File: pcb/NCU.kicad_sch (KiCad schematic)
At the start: 4 parts

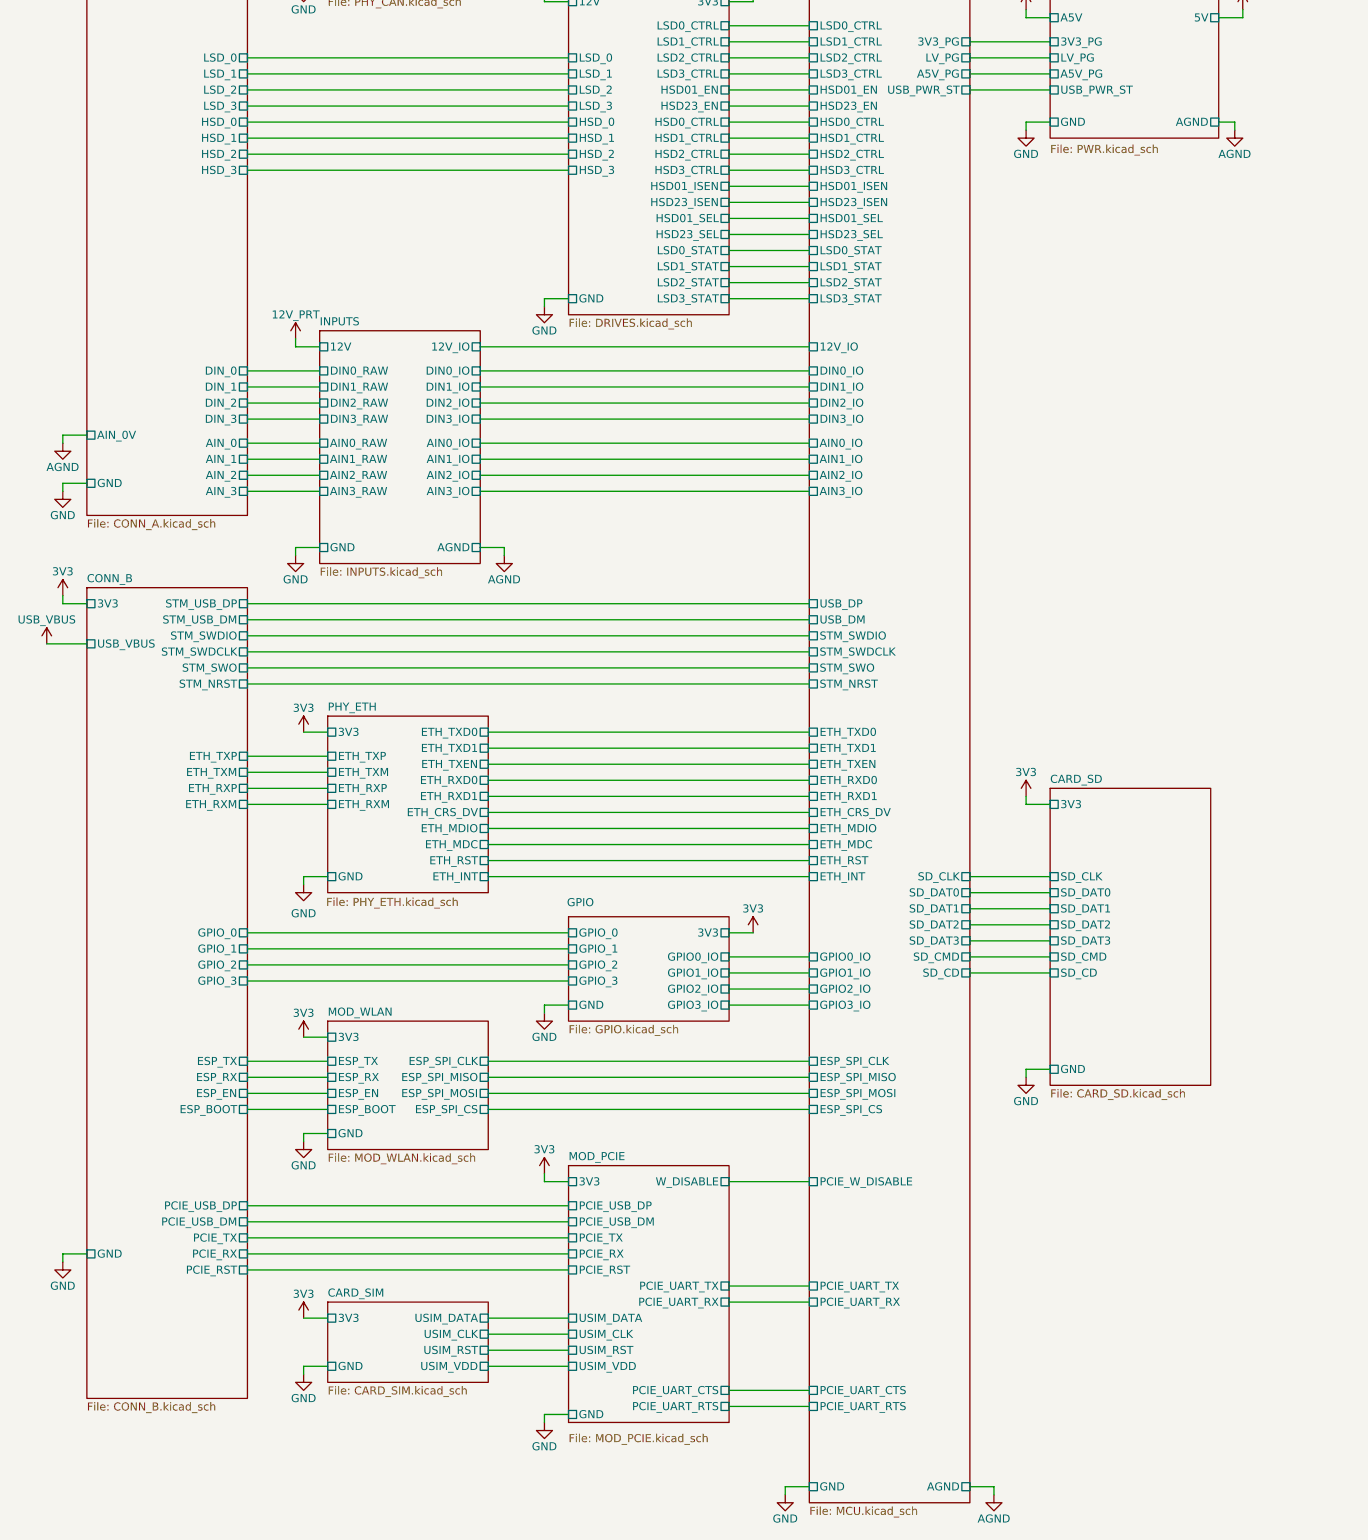
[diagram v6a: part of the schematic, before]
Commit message: removed AGND and added ground garden
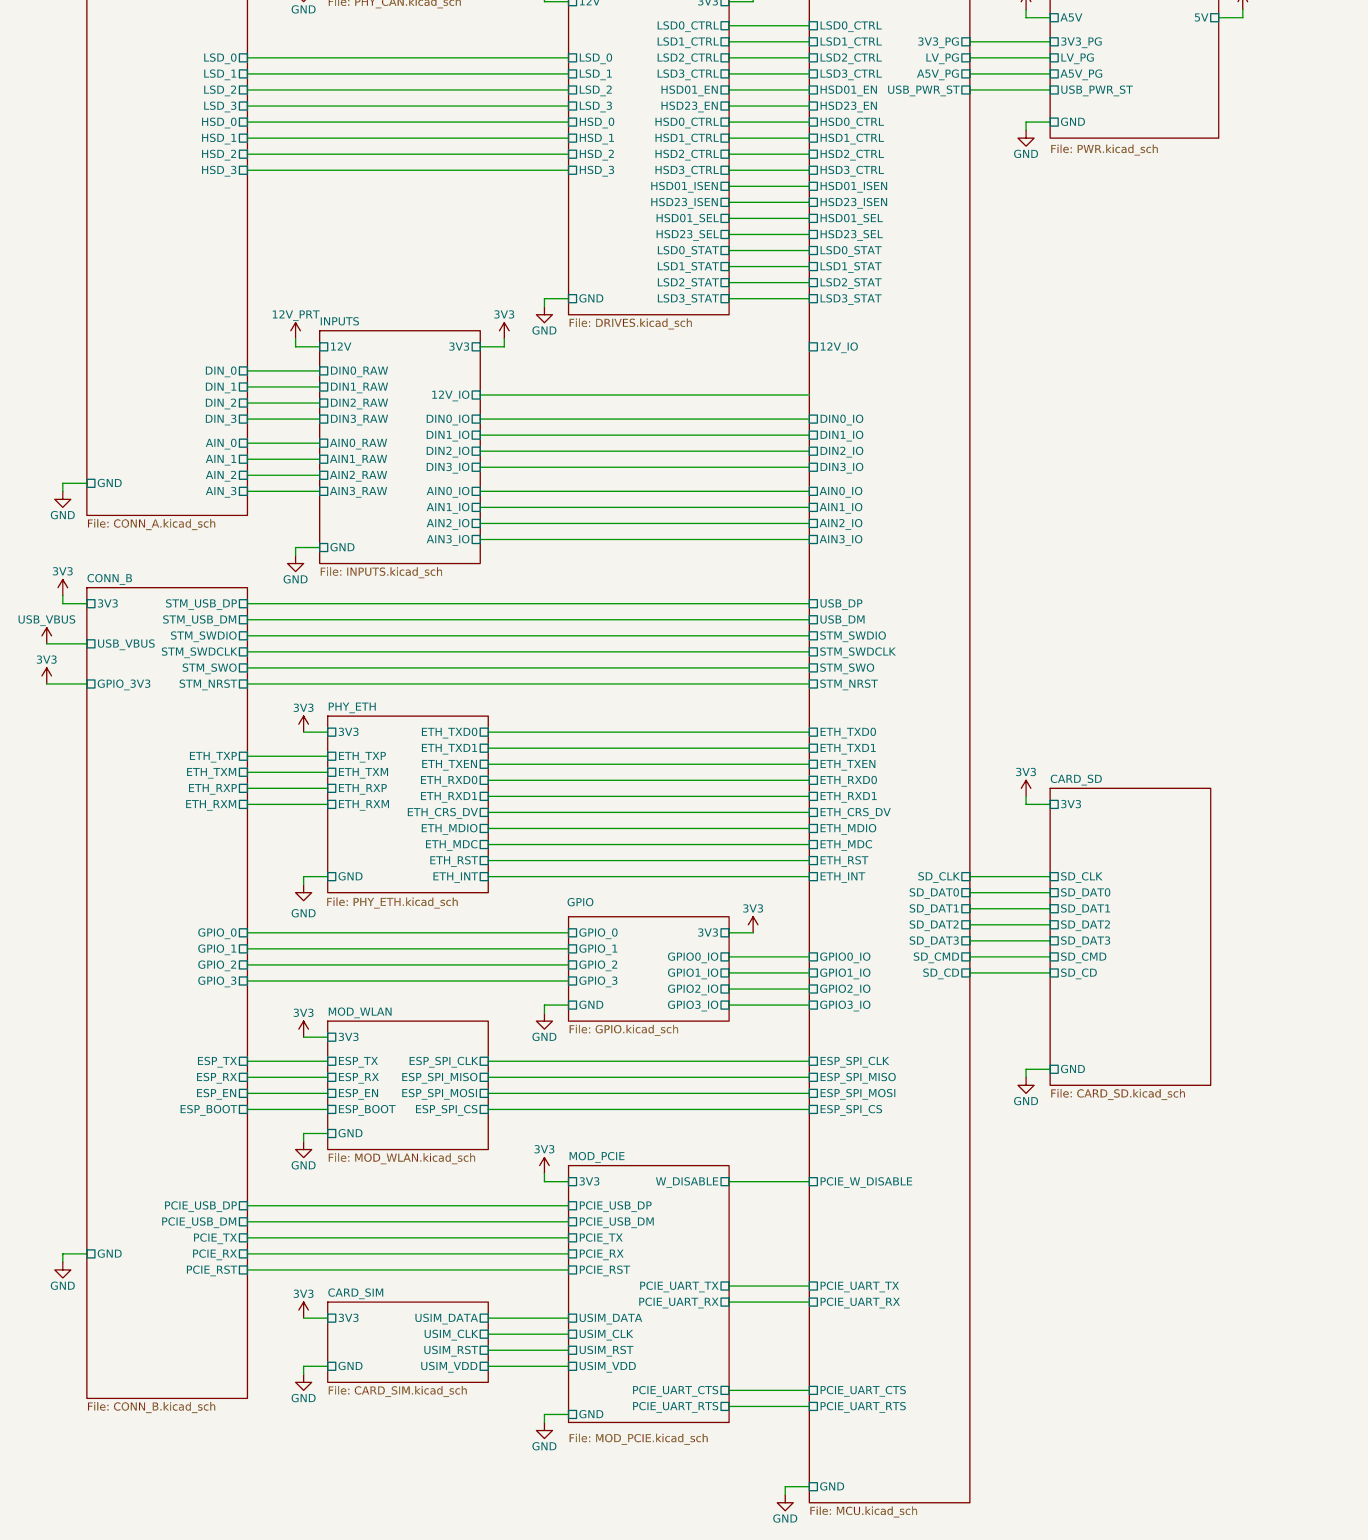
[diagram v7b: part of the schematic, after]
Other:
- sheet CONN_A ports: added none; removed AIN_0V
- sheet CONN_B ports: added GPIO_3V3; removed none
- sheet INPUTS ports: added 3V3; removed AGND
- sheet MCU ports: added none; removed AGND
- sheet PWR ports: added none; removed AGND
